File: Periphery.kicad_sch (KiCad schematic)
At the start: 27 parts, among them SW1 Mitsumi R-667996, SW2 Mitsumi R-667996, U2 SN74LV595A, U3 THVD1420DRLR, U4 TPS2521ARPWR, U5 SN74LV595A, U6 TS5A3159DCK

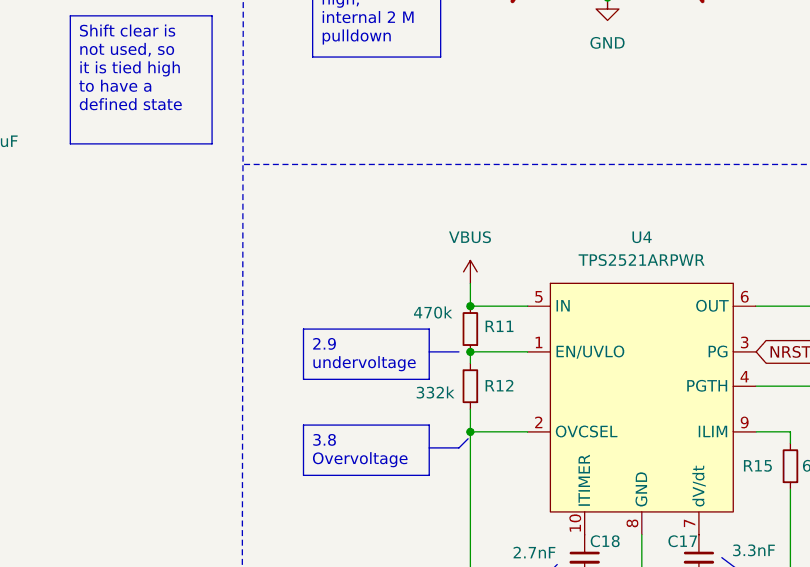
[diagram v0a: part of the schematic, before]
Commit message: Fixed ERC power flag issues
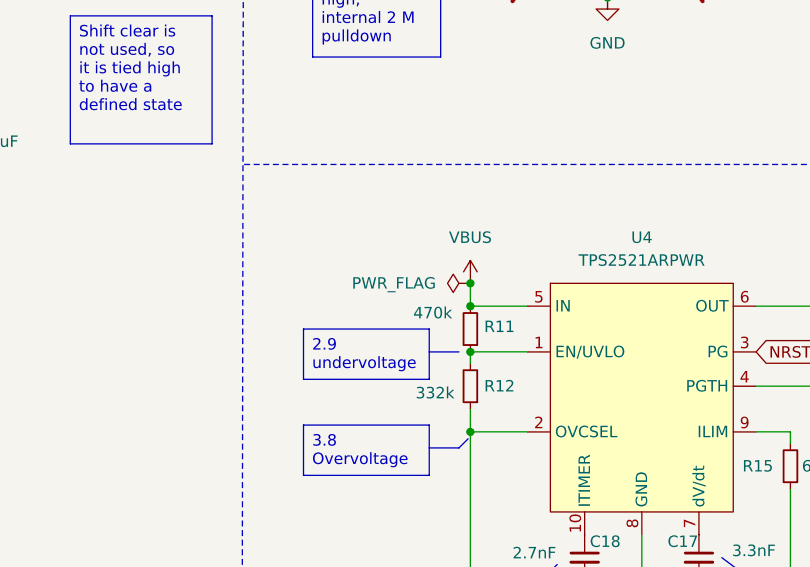
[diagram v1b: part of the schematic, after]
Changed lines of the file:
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@@
+	)
+	(junction
+		(at 132.08 129.54)
+		(diameter 0)
+		(color 0 0 0 0)
 	)
 	(junction
@@
 					(unit 1)
 				)
+			)
+		)
+	)
+	(symbol
+		(lib_id "power:PWR_FLAG")
+		(at 132.08 129.54 90)
+		(unit 1)
+		(exclude_from_sim no)
+		(in_bom yes)
+		(on_board yes)
+		(dnp no)
+		(fields_autoplaced yes)
+		(property "Reference" "#FLG02"
+			(at 130.175 129.54 0)
+			(effects
+				(font
+					(size 1.27 1.27)
+				)
+				(hide yes)
+			)
+		)
+		(property "Value" "PWR_FLAG"
+			(at 128.27 129.5399 90)
+			(effects
+				(font
+					(size 1.27 1.27)
+				)
+				(justify left)
+			)
+		)
+		(property "Footprint" ""
+			(at 132.08 129.54 0)
+			(effects
+				(font
+					(size 1.27 1.27)
+				)
+				(hide yes)
+			)
+		)
+		(property "Datasheet" "~"
+			(at 132.08 129.54 0)
+			(effects
+				(font
+					(size 1.27 1.27)
+				)
+				(hide yes)
+			)
+		)
+		(property "Description" "Special symbol for telling ERC where power comes from"
+			(at 132.08 129.54 0)
+			(effects
+				(font
+					(size 1.27 1.27)
+				)
+				(hide yes)
+			)
+		)
+		(pin "1"
+		)
+		(instances
+			(project "ESP32-S3 Hub"
+				(path "/a8c80fba-3bca-4358-b5bb-9ebf9383c658/c12991ca-4617-4c32-8678-9934d12b2f96"
+					(reference "#FLG02")
+					(unit 1)
+				)

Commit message: Updated schematic symbols
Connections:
- net GND: no longer U2.17 (GND), U5.17 (GND)
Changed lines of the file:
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@@
 		(pin "1"
-		)
-		(pin "17"
 		)
 		(instances
@@
 	)
 	(symbol
-		(lib_name "74HC595_1")
 		(lib_id "74xx:74HC595")
 		(at 54.61 87.63 0)
@@
 		)
 		(pin "1"
-		)
-		(pin "17"
 		)
 		(instances
@@
 			(effects
 				(font
+					(size 1.27 1.27)
+				)
+				(hide yes)
+			)
+		)
+		(property "Sim.Pins" "1=K 2=A"
+			(at 96.52 30.48 0)
+			(effects
+				(font

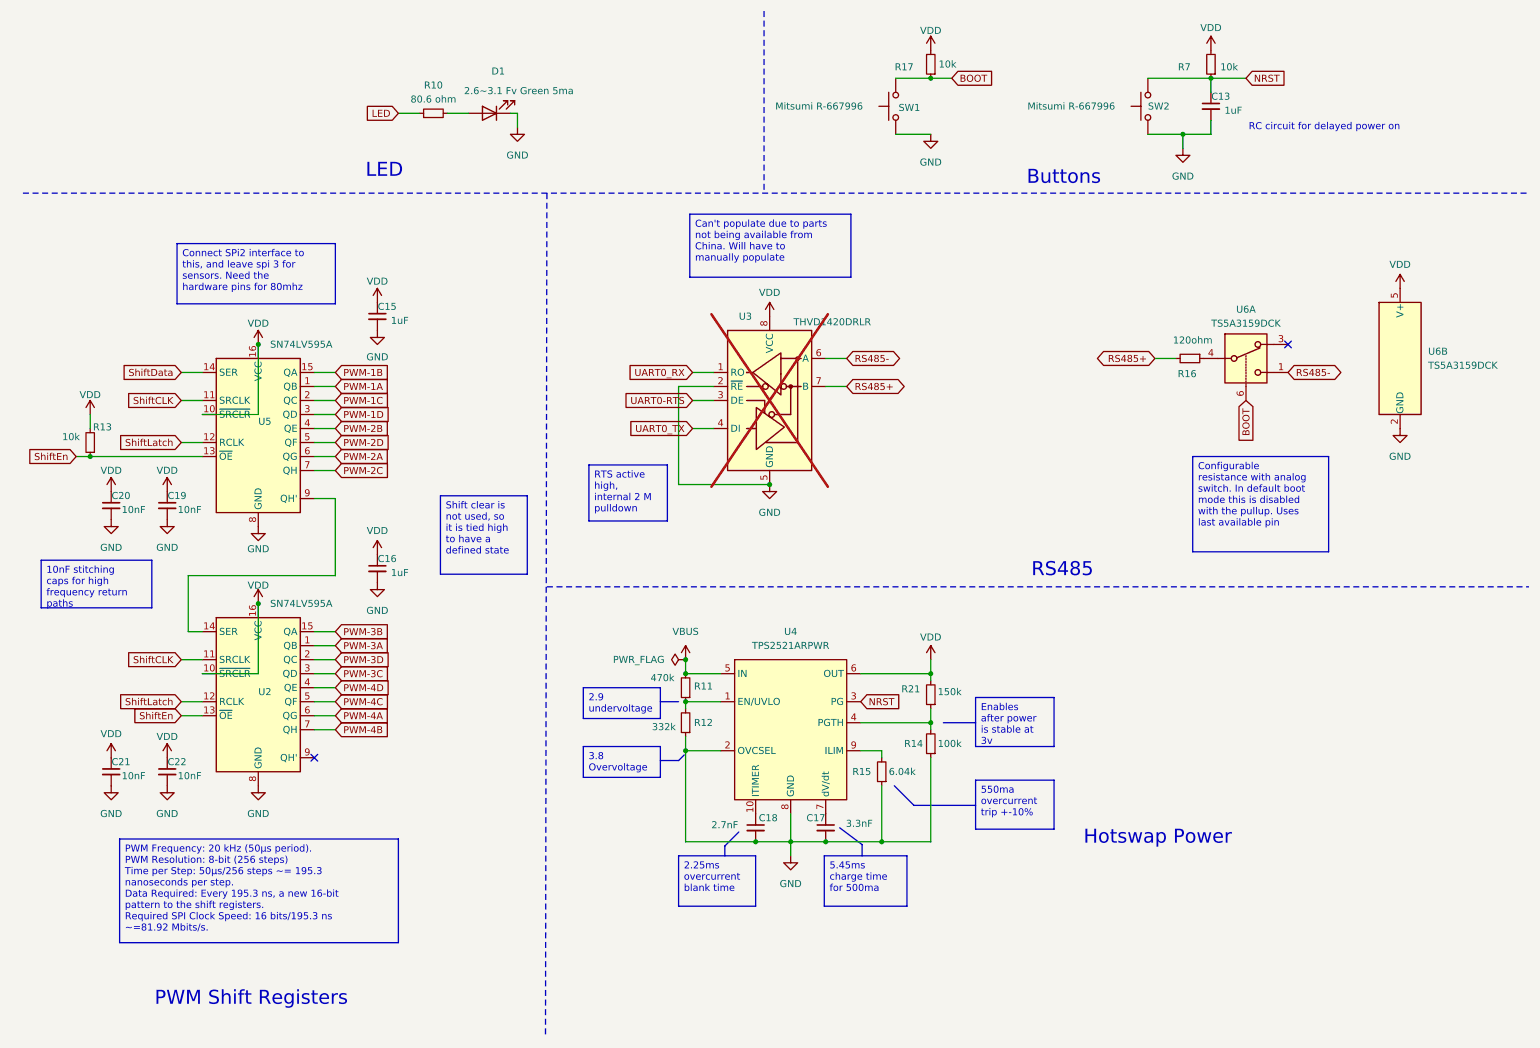
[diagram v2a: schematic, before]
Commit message: Fixed typos with ADC-4 pins, split a few circuits
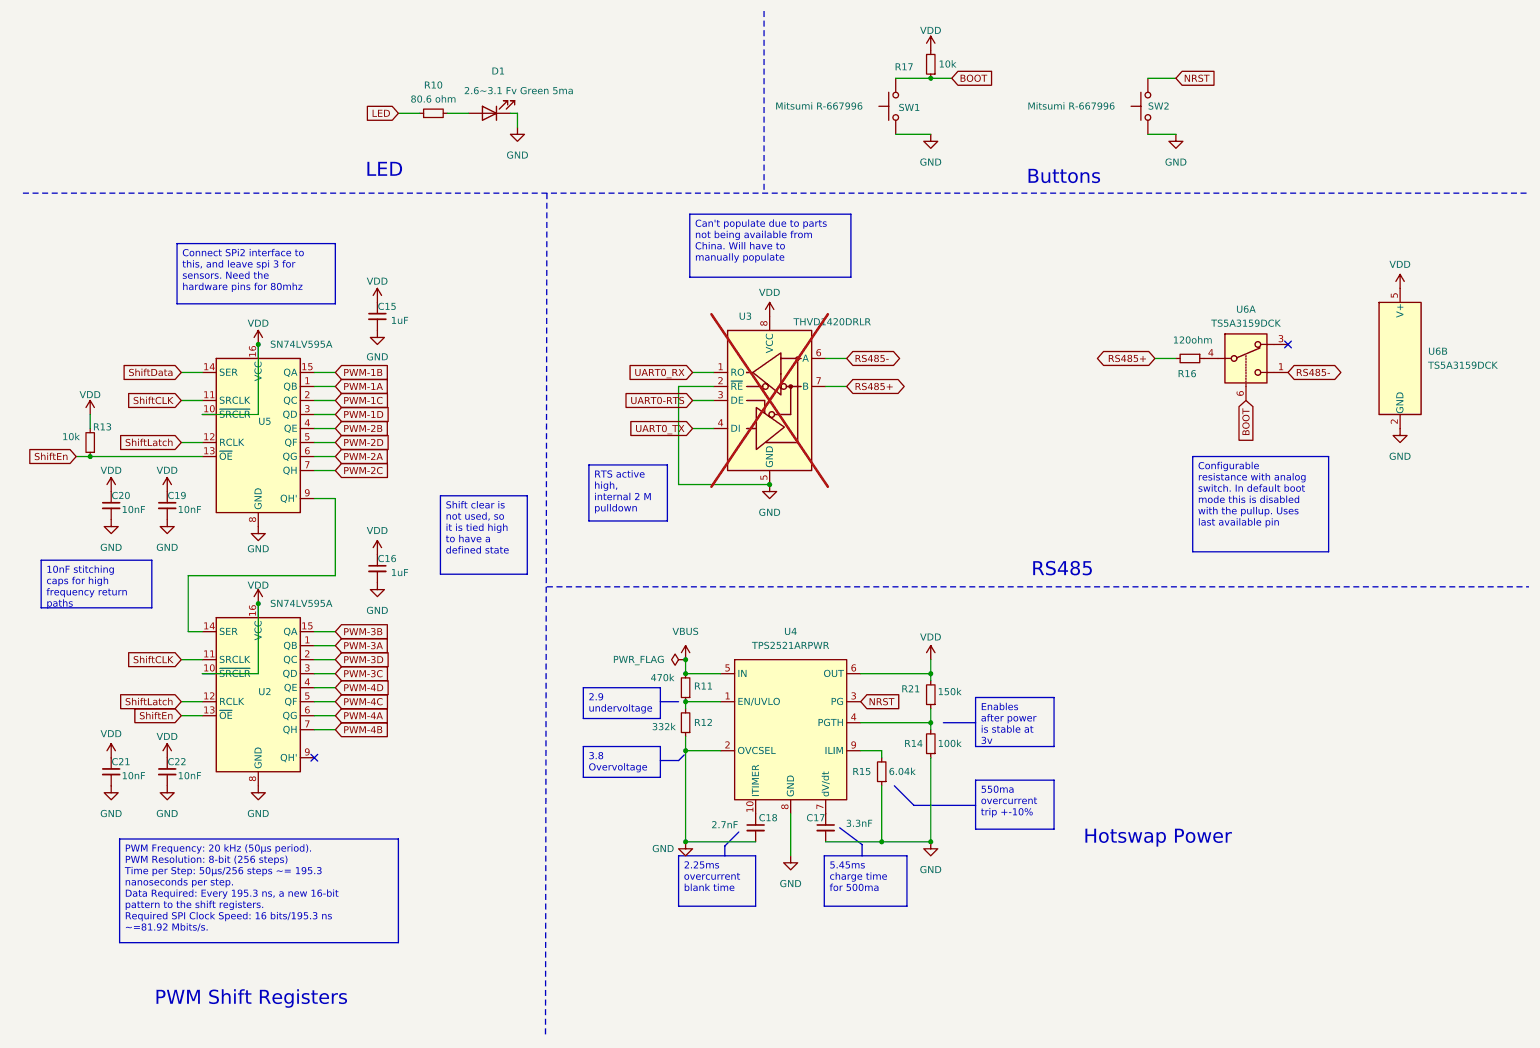
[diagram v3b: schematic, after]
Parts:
- removed C13: 1uF, Capacitor_SMD:C_0402_1005Metric, symbol Device:C_Small
- removed R7: 10k, Resistor_SMD:R_0402_1005Metric, symbol Device:R_Small
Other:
- note removed: "RC circuit for delayed power on"

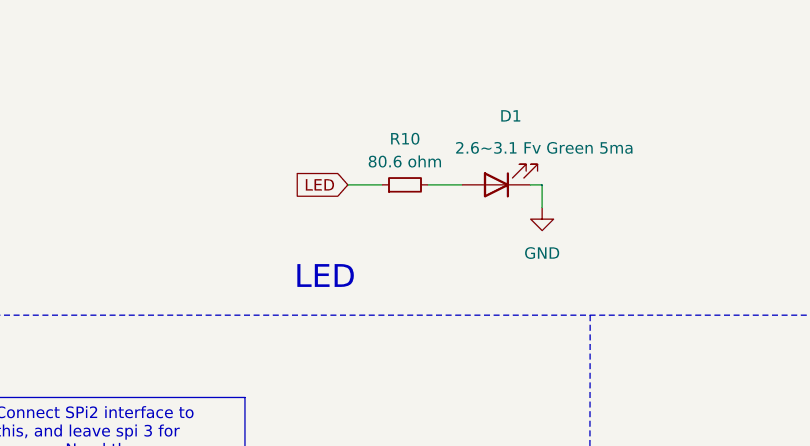
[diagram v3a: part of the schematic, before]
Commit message: Changed LED resistor value to be more standard, reduce brightness
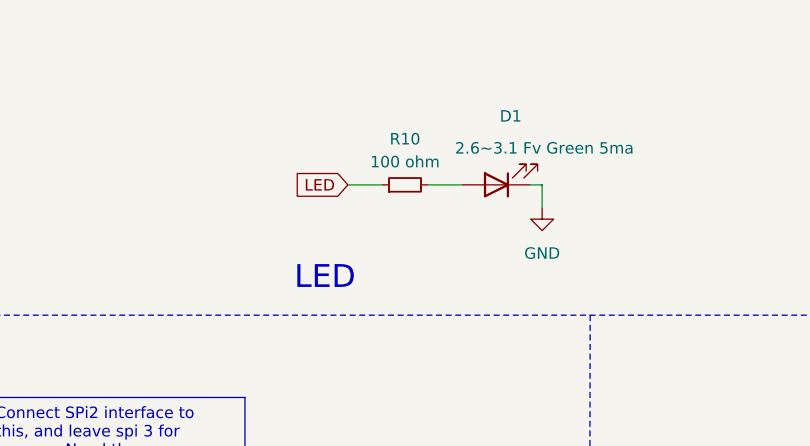
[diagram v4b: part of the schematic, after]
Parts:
- R10: value 80.6 ohm -> 100 ohm
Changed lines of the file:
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@@
 			)
 		)
-		(property "Value" "80.6 ohm"
+		(property "Value" "100 ohm"
 			(at 86.36 27.94 90)
 			(effects

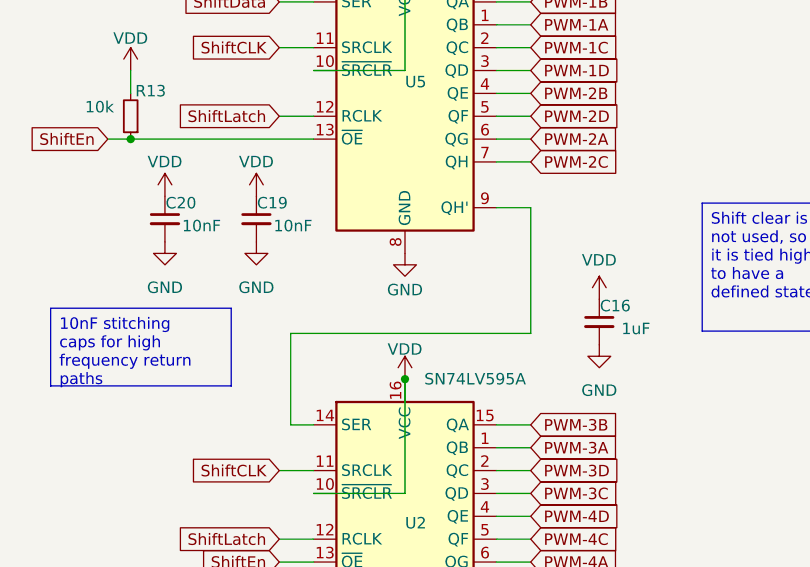
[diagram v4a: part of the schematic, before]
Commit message: Fixed symbol issue with shift register
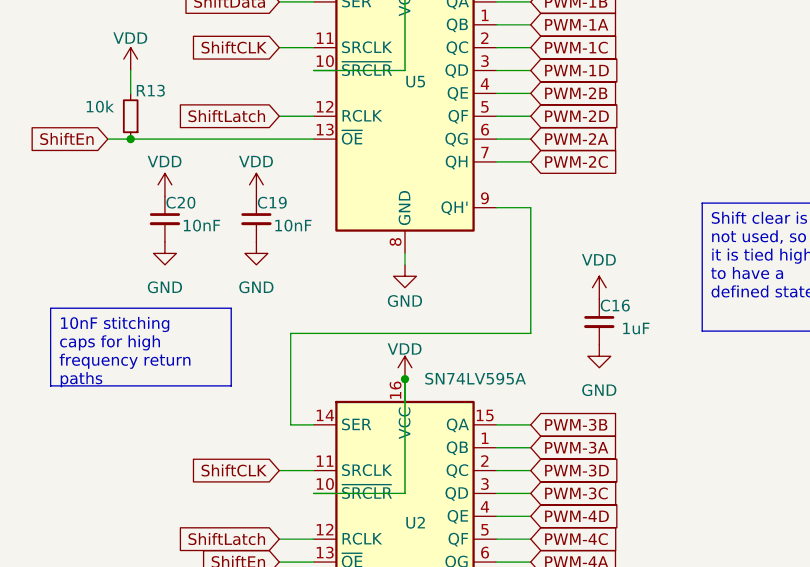
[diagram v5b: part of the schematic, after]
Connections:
- net GND renamed 17
- net 17: now also U2.17, U5.17

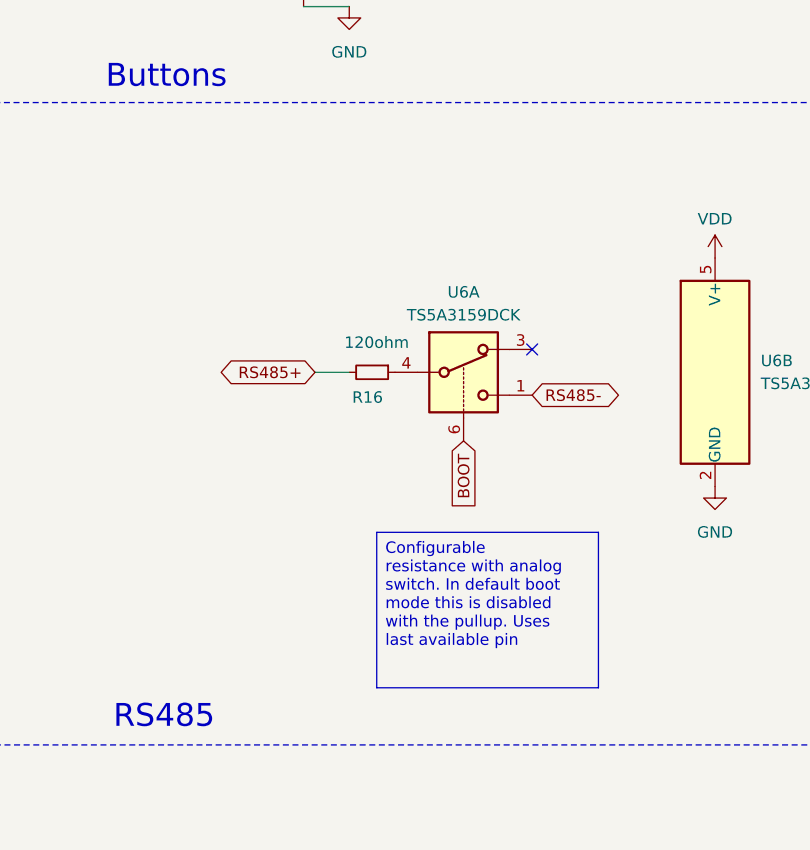
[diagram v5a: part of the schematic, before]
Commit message: Changed configurable resistor pin in schematic
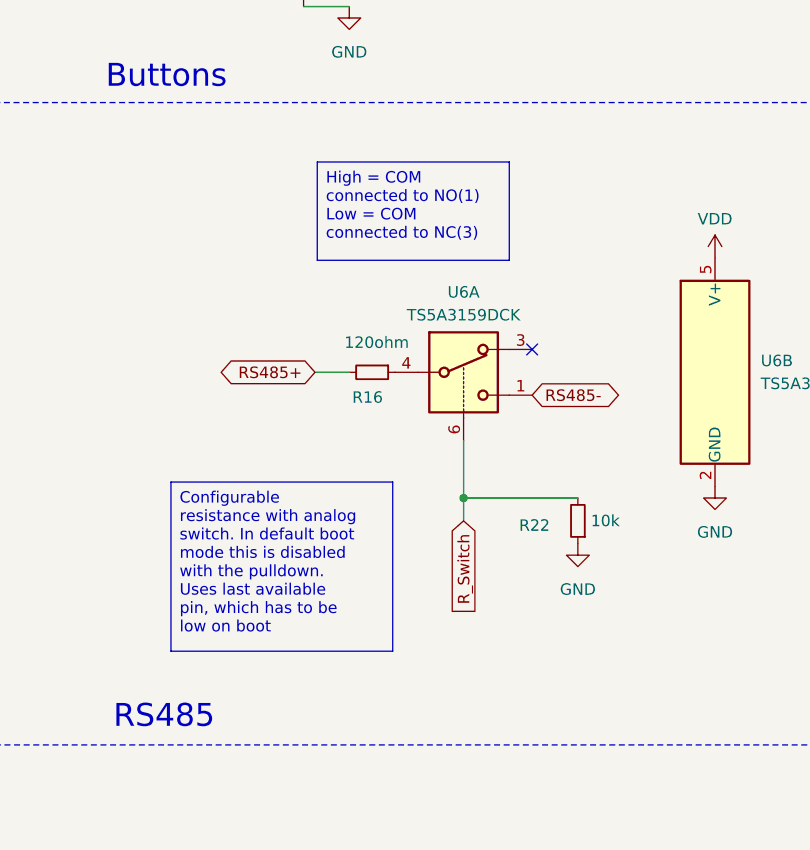
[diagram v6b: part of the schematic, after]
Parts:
- added R22: 10k, Resistor_SMD:R_0402_1005Metric, symbol Device:R_Small
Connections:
- net 17: now also R22.1
- net BOOT: no longer U6.6
- new net R_Switch: R22.2, U6.6
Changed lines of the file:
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@@
 		)
 	)
+	(text_box "High = COM connected to NO(1)\nLow = COM connected to NC(3)"
+		(exclude_from_sim no)
+		(at 217.424 51.562 0)
+		(size 21.336 10.922)
+		(margins 0.9525 0.9525 0.9525 0.9525)
+		(stroke
+			(width 0)
+			(type solid)
+		)
+		(fill
+			(type none)
+		)
+		(effects
+			(font
+				(size 1.27 1.27)
+			)
+			(justify left top)
+		)
+	)
 	(text_box "RTS active high, internal 2 M pulldown"
 		(exclude_from_sim no)
@@
 		)
 	)
-	(text_box "Configurable resistance with analog switch. In default boot mode this is disabled with the pullup. Uses last available pin"
+	(text_box "Configurable resistance with analog switch. In default boot mode this is disabled with the pulldown. Uses last available pin, which has to be low on boot"
 		(exclude_from_sim no)
-		(at 224.028 92.71 0)
-		(size 24.638 17.272)
+		(at 201.168 87.122 0)
+		(size 24.638 18.796)
 		(margins 0.9525 0.9525 0.9525 0.9525)
 		(stroke
@@
 	)
 	(junction
+		(at 233.68 88.9)
+		(diameter 0)
+		(color 0 0 0 0)
+	)
+	(junction
 		(at 132.08 132.08)
 		(diameter 0)
@@
 	(wire
 		(pts
+			(xy 233.68 91.44) (xy 233.68 88.9)
+		)
+		(stroke
+			(width 0)
+			(type default)
+		)
+	)
+	(wire
+		(pts
 			(xy 132.08 132.08) (xy 138.43 132.08)
 		)
@@
 	(wire
 		(pts
+			(xy 233.68 88.9) (xy 233.68 82.55)
+		)
+		(stroke
+			(width 0)
+			(type default)
+		)
+	)
+	(wire
+		(pts
 			(xy 68.58 137.16) (xy 64.77 137.16)
 		)
@@
 	(wire
 		(pts
+			(xy 233.68 88.9) (xy 246.38 88.9)
+		)
+		(stroke
+			(width 0)
+			(type default)
+		)
+	)
+	(wire
+		(pts
 			(xy 100.33 30.48) (xy 101.6 30.48)
 		)
@@
 		)
 	)
+	(global_label "R_Switch"
+		(shape input)
+		(at 233.68 91.44 270)
+		(fields_autoplaced yes)
+		(effects
+			(font
+				(size 1.27 1.27)
+			)
+			(justify right)
+		)
+		(property "Intersheetrefs" "${INTERSHEET_REFS}"
+			(at 233.68 102.7709 90)
+			(effects
+				(font
+					(size 1.27 1.27)
+				)
+				(justify right)
+				(hide yes)
+			)
+		)
+	)
 	(global_label "PWM-3A"
 		(shape input)
@@
 		)
 	)
-	(global_label "BOOT"
-		(shape input)
-		(at 233.68 82.55 270)
-		(fields_autoplaced yes)
-		(effects
-			(font
-				(size 1.27 1.27)
-			)
-			(justify right)
-		)
-		(property "Intersheetrefs" "${INTERSHEET_REFS}"
-			(at 233.68 90.4338 90)
-			(effects
-				(font
-					(size 1.27 1.27)
-				)
-				(justify right)
-				(hide yes)
-			)
-		)
-	)
 	(global_label "RS485-"
 		(shape bidirectional)
@@
 					(unit 1)
 				)
+			)
+		)
+	)
+	(symbol
+		(lib_id "Device:R_Small")
+		(at 246.38 91.44 180)
+		(unit 1)
+		(exclude_from_sim no)
+		(in_bom yes)
+		(on_board yes)
+		(dnp no)
+		(property "Reference" "R22"
+			(at 241.554 91.948 0)
+			(effects
+				(font
+					(size 1.27 1.27)
+				)
+			)
+		)
+		(property "Value" "10k"
+			(at 249.428 91.44 0)
+			(effects
+				(font
+					(size 1.27 1.27)
+				)
+			)
+		)
+		(property "Footprint" "Resistor_SMD:R_0402_1005Metric"
+			(at 246.38 91.44 0)
+			(effects
+				(font
+					(size 1.27 1.27)
+				)
+				(hide yes)
+			)
+		)
+		(property "Datasheet" "~"
+			(at 246.38 91.44 0)
+			(effects
+				(font
+					(size 1.27 1.27)
+				)
+				(hide yes)
+			)
+		)
+		(property "Description" "Resistor, small symbol"
+			(at 246.38 91.44 0)
+			(effects
+				(font
+					(size 1.27 1.27)
+				)
+				(hide yes)
+			)
+		)
+		(property "LCSC" "C25744"
+			(at 241.554 91.948 0)
+			(effects
+				(font
+					(size 1.27 1.27)
+				)
+				(hide yes)
+			)
+		)
+		(pin "2"
+		)
+		(pin "1"
+		)
+		(instances
+			(project "ESP32-S3 Hub"
+				(path "/a8c80fba-3bca-4358-b5bb-9ebf9383c658/c12991ca-4617-4c32-8678-9934d12b2f96"
+					(reference "R22")
+					(unit 1)
+				)
+			)
+		)
+	)
+	(symbol
+		(lib_id "power:GND")
+		(at 246.38 93.98 0)
+		(unit 1)
+		(exclude_from_sim no)
+		(in_bom yes)
+		(on_board yes)
+		(dnp no)
+		(fields_autoplaced yes)
+		(property "Reference" "#PWR043"
+			(at 246.38 100.33 0)
+			(effects
+				(font
+					(size 1.27 1.27)
+				)
+				(hide yes)
+			)
+		)
+		(property "Value" "GND"
+			(at 246.38 99.06 0)
+			(effects
+				(font
+					(size 1.27 1.27)
+				)
+			)
+		)
+		(property "Footprint" ""
+			(at 246.38 93.98 0)
+			(effects
+				(font
+					(size 1.27 1.27)
+				)
+				(hide yes)
+			)
+		)
+		(property "Datasheet" ""
+			(at 246.38 93.98 0)
+			(effects
+				(font
+					(size 1.27 1.27)
+				)
+				(hide yes)
+			)
+		)
+		(property "Description" "Power symbol creates a global label with name \"GND\" , ground"
+			(at 246.38 93.98 0)
+			(effects
+				(font
+					(size 1.27 1.27)
+				)
+				(hide yes)
+			)
+		)
+		(pin "1"
+		)
+		(instances
+			(project "ESP32-S3 Hub"
+				(path "/a8c80fba-3bca-4358-b5bb-9ebf9383c658/c12991ca-4617-4c32-8678-9934d12b2f96"
+					(reference "#PWR043")
+					(unit 1)
+				)
